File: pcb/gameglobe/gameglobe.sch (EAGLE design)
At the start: 12 parts

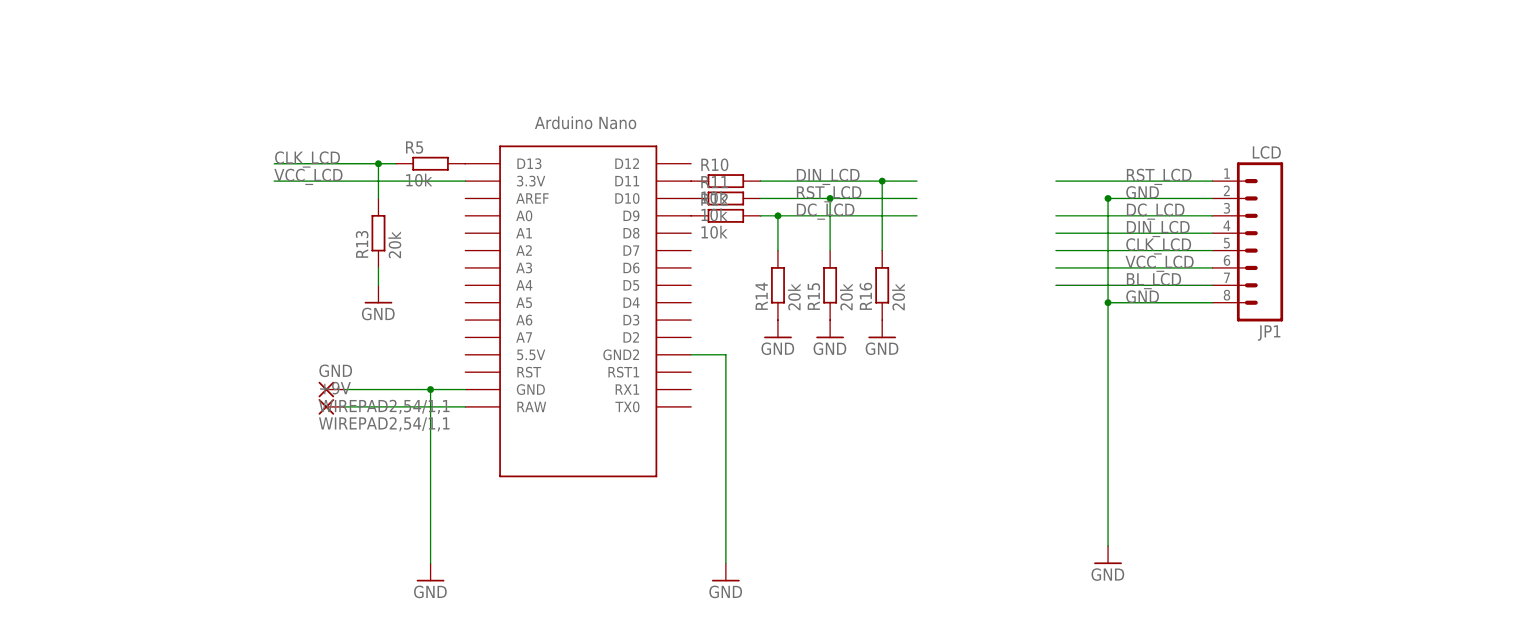
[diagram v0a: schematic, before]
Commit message: BOM is sortof complete, and PCB is more complete-ish now
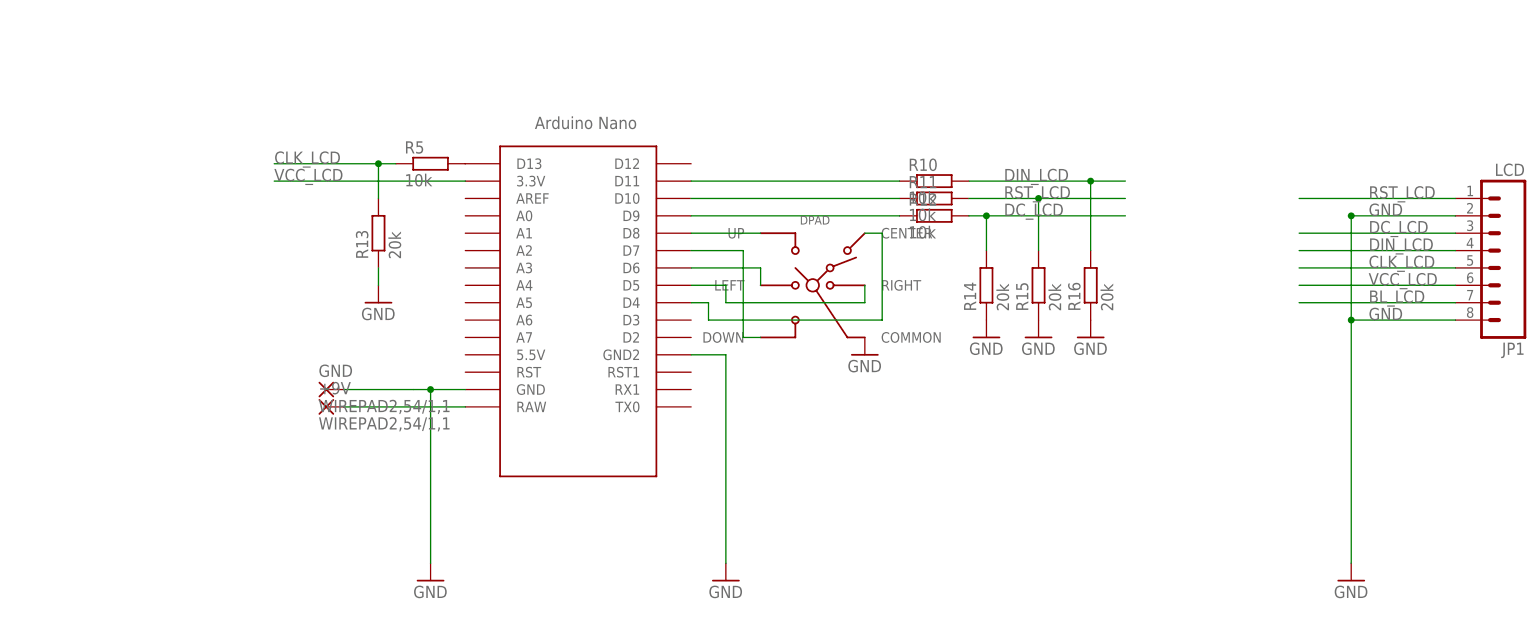
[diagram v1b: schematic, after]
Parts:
- added DPAD: SKQUCAA010, gamaral:SKQUCAA010
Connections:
- new net N$10: DPAD.CENTER, U$1.D4
- new net N$5: DPAD.UP, U$1.D8
- new net N$6: DPAD.DOWN, U$1.D7
- new net N$8: DPAD.LEFT, U$1.D6
- new net N$9: DPAD.RIGHT, U$1.D5
- net GND: now also DPAD.COMMON
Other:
- moved on the sheet: JP1, R10, R11, R12, R14, R15, R16

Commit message: Add backlight wire and resistor
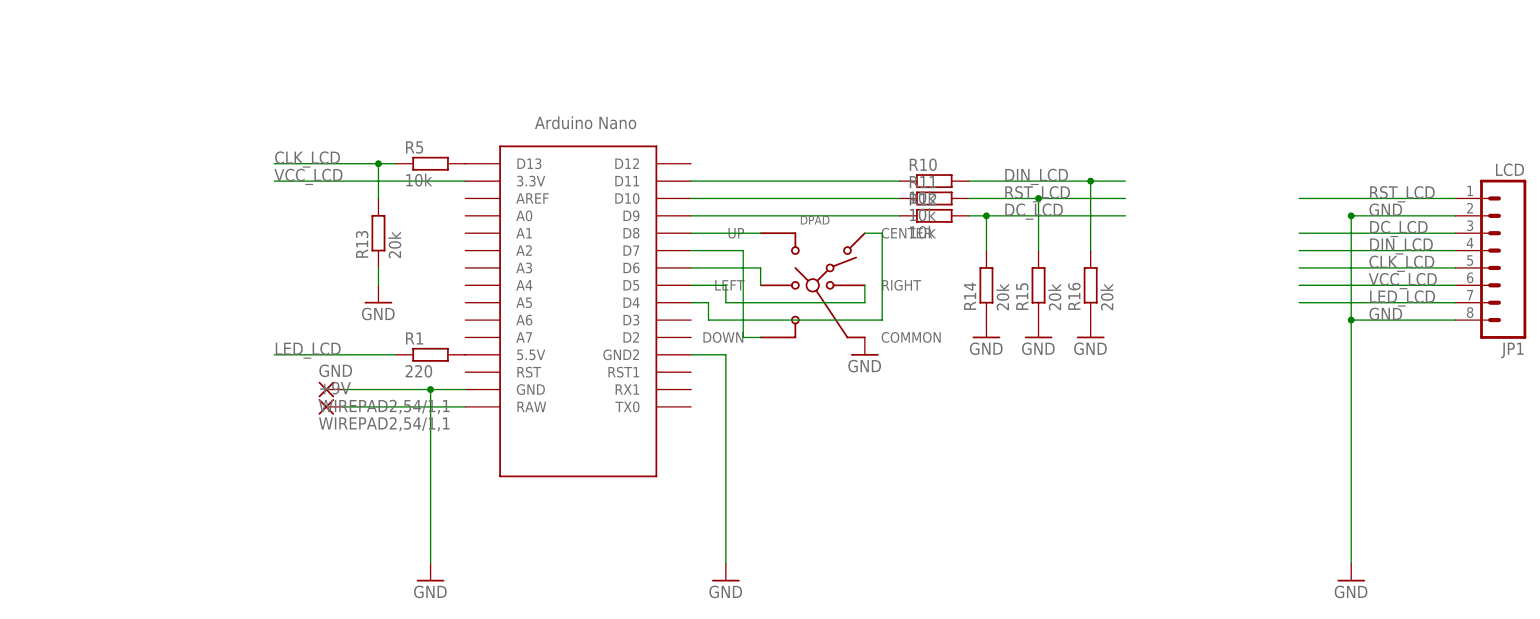
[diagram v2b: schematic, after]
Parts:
- added R1: 220, resistor:R-EU_0207/10
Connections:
- removed net BL_LCD: JP1.7
- new net LED_LCD: JP1.7, R1.1
- new net N$11: R1.2, U$1.5.5V
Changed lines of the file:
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@@
 <part name="DPAD" library="gamaral" deviceset="SKQU" device="CAA010"/>
 <part name="GND8" library="supply1" deviceset="GND" device=""/>
+<part name="R1" library="resistor" deviceset="R-EU_" device="0207/10" value="220"/>
 </parts>
 <sheets>
@@
 <instance part="DPAD" gate="Q$1" x="88.9" y="50.8"/>
 <instance part="GND8" gate="1" x="96.52" y="40.64"/>
+<instance part="R1" gate="G$1" x="33.02" y="40.64"/>
 </instances>
 <busses>
@@
 </segment>
 </net>
-<net name="BL_LCD" class="0">
+<net name="LED_LCD" class="0">
 <segment>
 <pinref part="JP1" gate="G$1" pin="7"/>
 <wire x1="182.88" y1="48.26" x2="160.02" y2="48.26" width="0.1524" layer="91"/>
 <label x="170.18" y="48.26" size="1.778" layer="95"/>
+</segment>
+<segment>
+<pinref part="R1" gate="G$1" pin="1"/>
+<wire x1="27.94" y1="40.64" x2="10.16" y2="40.64" width="0.1524" layer="91"/>
+<label x="10.16" y="40.64" size="1.778" layer="95"/>
 </segment>
 </net>
@@
 </segment>
 </net>
+<net name="N$11" class="0">
+<segment>
+<pinref part="U$1" gate="G$1" pin="5.5V"/>
+<pinref part="R1" gate="G$1" pin="2"/>
+</segment>
+</net>

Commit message: Improve net names and board layout
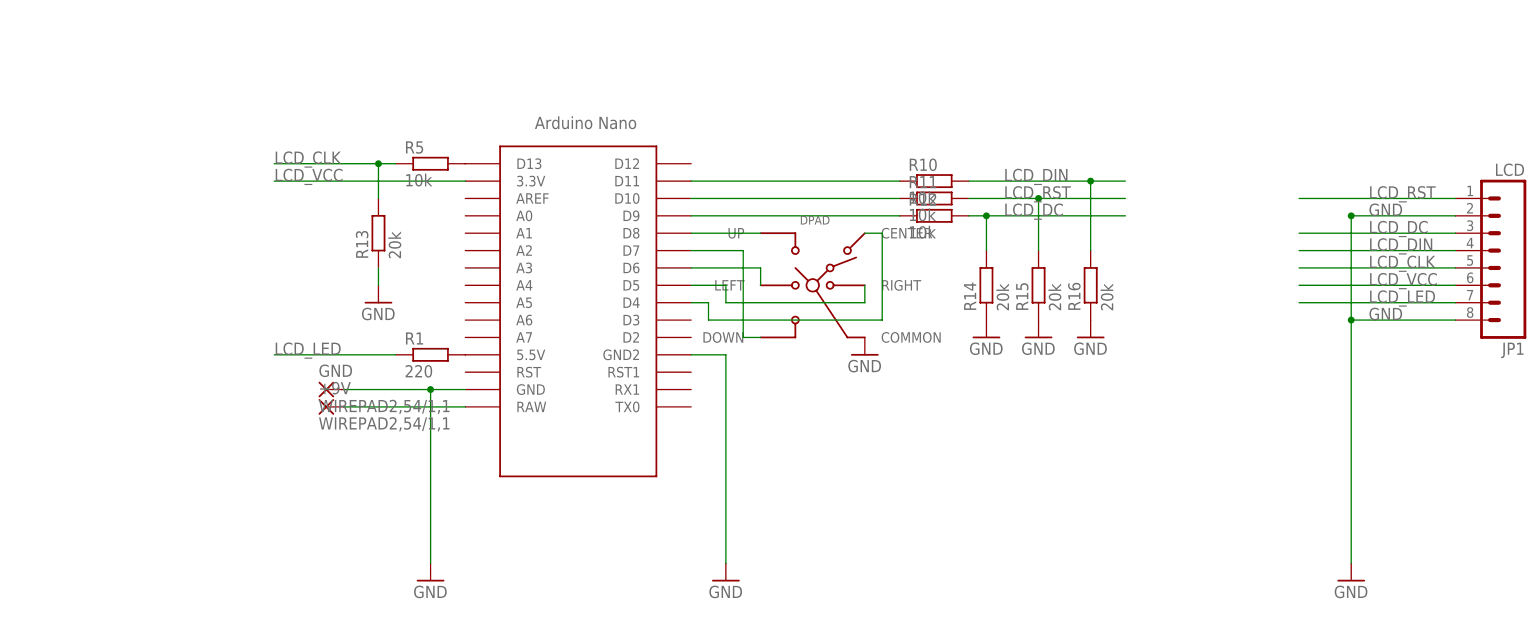
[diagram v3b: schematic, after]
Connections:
- net CLK_LCD renamed LCD_CLK
- net DC_LCD renamed LCD_DC
- net DIN_LCD renamed LCD_DIN
- net LED_LCD renamed LCD_LED
- net N$10 renamed DPAD_CENTER
- net N$5 renamed DPAD_UP
- net N$6 renamed DPAD_DOWN
- net N$8 renamed DPAD_LEFT
- net N$9 renamed DPAD_RIGHT
- net RST_LCD renamed LCD_RST
- net VCC_LCD renamed LCD_VCC
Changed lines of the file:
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@@
 </segment>
 </net>
-<net name="RST_LCD" class="0">
+<net name="LCD_RST" class="0">
 <segment>
 <pinref part="JP1" gate="G$1" pin="1"/>
@@
 </segment>
 </net>
-<net name="DC_LCD" class="0">
+<net name="LCD_DC" class="0">
 <segment>
 <pinref part="JP1" gate="G$1" pin="3"/>
@@
 </segment>
 </net>
-<net name="DIN_LCD" class="0">
+<net name="LCD_DIN" class="0">
 <segment>
 <pinref part="JP1" gate="G$1" pin="4"/>
@@
 </segment>
 </net>
-<net name="CLK_LCD" class="0">
+<net name="LCD_CLK" class="0">
 <segment>
 <pinref part="JP1" gate="G$1" pin="5"/>
@@
 </segment>
 </net>
-<net name="VCC_LCD" class="0">
+<net name="LCD_VCC" class="0">
 <segment>
 <pinref part="JP1" gate="G$1" pin="6"/>
@@
 </segment>
 </net>
-<net name="LED_LCD" class="0">
+<net name="LCD_LED" class="0">
 <segment>
 <pinref part="JP1" gate="G$1" pin="7"/>
@@
 </segment>
 </net>
-<net name="N$5" class="0">
+<net name="DPAD_UP" class="0">
 <segment>
 <pinref part="U$1" gate="G$1" pin="D8"/>
@@
 </segment>
 </net>
-<net name="N$6" class="0">
+<net name="DPAD_DOWN" class="0">
 <segment>
 <pinref part="DPAD" gate="Q$1" pin="DOWN"/>
@@
 </segment>
 </net>
-<net name="N$8" class="0">
+<net name="DPAD_LEFT" class="0">
 <segment>
 <pinref part="DPAD" gate="Q$1" pin="LEFT"/>
@@
 </segment>
 </net>
-<net name="N$9" class="0">
+<net name="DPAD_RIGHT" class="0">
 <segment>
 <pinref part="DPAD" gate="Q$1" pin="RIGHT"/>
@@
 </segment>
 </net>
-<net name="N$10" class="0">
+<net name="DPAD_CENTER" class="0">
 <segment>
 <pinref part="DPAD" gate="Q$1" pin="CENTER"/>

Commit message: Updated DRU file; Improved PCB layout; Added rounded edges and mount holes
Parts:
- renumbered U$1 to ARDUINO_NANO
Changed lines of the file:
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@@
 </classes>
 <parts>
-<part name="U$1" library="Arduino-clone" deviceset="NANO" device=""/>
+<part name="ARDUINO_NANO" library="Arduino-clone" deviceset="NANO" device=""/>
 <part name="+9V" library="wirepad" deviceset="WIREPAD" device="2,54/1,1"/>
 <part name="GND" library="wirepad" deviceset="WIREPAD" device="2,54/1,1"/>
@@
 </plain>
 <instances>
-<instance part="U$1" gate="G$1" x="60.96" y="53.34"/>
+<instance part="ARDUINO_NANO" gate="G$1" x="60.96" y="53.34"/>
 <instance part="+9V" gate="G$1" x="17.78" y="33.02"/>
 <instance part="GND" gate="G$1" x="17.78" y="35.56"/>
@@
 <net name="N$7" class="0">
 <segment>
-<pinref part="U$1" gate="G$1" pin="RAW"/>
+<pinref part="ARDUINO_NANO" gate="G$1" pin="RAW"/>
 <wire x1="38.1" y1="33.02" x2="20.32" y2="33.02" width="0.1524" layer="91"/>
 <pinref part="+9V" gate="G$1" pin="P"/>
@@
 <segment>
 <pinref part="GND1" gate="1" pin="GND"/>
-<pinref part="U$1" gate="G$1" pin="GND2"/>
+<pinref part="ARDUINO_NANO" gate="G$1" pin="GND2"/>
 <wire x1="71.12" y1="40.64" x2="76.2" y2="40.64" width="0.1524" layer="91"/>
 <wire x1="76.2" y1="40.64" x2="76.2" y2="10.16" width="0.1524" layer="91"/>
 </segment>
 <segment>
-<pinref part="U$1" gate="G$1" pin="GND"/>
+<pinref part="ARDUINO_NANO" gate="G$1" pin="GND"/>
 <wire x1="20.32" y1="35.56" x2="30.48" y2="35.56" width="0.1524" layer="91"/>
 <pinref part="GND2" gate="1" pin="GND"/>
@@
 </segment>
 <segment>
-<pinref part="U$1" gate="G$1" pin="3.3V"/>
+<pinref part="ARDUINO_NANO" gate="G$1" pin="3.3V"/>
 <label x="10.16" y="66.04" size="1.778" layer="95"/>
 <wire x1="38.1" y1="66.04" x2="10.16" y2="66.04" width="0.1524" layer="91"/>
@@
 <net name="N$1" class="0">
 <segment>
-<pinref part="U$1" gate="G$1" pin="D13"/>
+<pinref part="ARDUINO_NANO" gate="G$1" pin="D13"/>
 <pinref part="R5" gate="G$1" pin="2"/>
 </segment>
@@
 <net name="N$2" class="0">
 <segment>
-<pinref part="U$1" gate="G$1" pin="D11"/>
+<pinref part="ARDUINO_NANO" gate="G$1" pin="D11"/>
 <pinref part="R10" gate="G$1" pin="1"/>
 <wire x1="101.6" y1="66.04" x2="71.12" y2="66.04" width="0.1524" layer="91"/>
@@
 <net name="N$3" class="0">
 <segment>
-<pinref part="U$1" gate="G$1" pin="D10"/>
+<pinref part="ARDUINO_NANO" gate="G$1" pin="D10"/>
 <pinref part="R11" gate="G$1" pin="1"/>
 <wire x1="101.6" y1="63.5" x2="71.12" y2="63.5" width="0.1524" layer="91"/>
@@
 <net name="N$4" class="0">
 <segment>
-<pinref part="U$1" gate="G$1" pin="D9"/>
+<pinref part="ARDUINO_NANO" gate="G$1" pin="D9"/>
 <pinref part="R12" gate="G$1" pin="1"/>
 <wire x1="101.6" y1="60.96" x2="71.12" y2="60.96" width="0.1524" layer="91"/>
@@
 <net name="DPAD_UP" class="0">
 <segment>
-<pinref part="U$1" gate="G$1" pin="D8"/>
+<pinref part="ARDUINO_NANO" gate="G$1" pin="D8"/>
 <pinref part="DPAD" gate="Q$1" pin="UP"/>
 <wire x1="71.12" y1="58.42" x2="81.28" y2="58.42" width="0.1524" layer="91"/>
@@
 <wire x1="81.28" y1="43.18" x2="78.74" y2="43.18" width="0.1524" layer="91"/>
 <wire x1="78.74" y1="43.18" x2="78.74" y2="55.88" width="0.1524" layer="91"/>
-<pinref part="U$1" gate="G$1" pin="D7"/>
+<pinref part="ARDUINO_NANO" gate="G$1" pin="D7"/>
 <wire x1="78.74" y1="55.88" x2="71.12" y2="55.88" width="0.1524" layer="91"/>
 </segment>
@@
 <pinref part="DPAD" gate="Q$1" pin="LEFT"/>
 <wire x1="81.28" y1="50.8" x2="81.28" y2="53.34" width="0.1524" layer="91"/>
-<pinref part="U$1" gate="G$1" pin="D6"/>
+<pinref part="ARDUINO_NANO" gate="G$1" pin="D6"/>
 <wire x1="81.28" y1="53.34" x2="71.12" y2="53.34" width="0.1524" layer="91"/>
 </segment>
@@
 <wire x1="96.52" y1="48.26" x2="76.2" y2="48.26" width="0.1524" layer="91"/>
 <wire x1="76.2" y1="48.26" x2="76.2" y2="50.8" width="0.1524" layer="91"/>
-<pinref part="U$1" gate="G$1" pin="D5"/>
+<pinref part="ARDUINO_NANO" gate="G$1" pin="D5"/>
 <wire x1="76.2" y1="50.8" x2="71.12" y2="50.8" width="0.1524" layer="91"/>
 </segment>
@@
 <wire x1="99.06" y1="45.72" x2="73.66" y2="45.72" width="0.1524" layer="91"/>
 <wire x1="73.66" y1="45.72" x2="73.66" y2="48.26" width="0.1524" layer="91"/>
-<pinref part="U$1" gate="G$1" pin="D4"/>
+<pinref part="ARDUINO_NANO" gate="G$1" pin="D4"/>
 <wire x1="73.66" y1="48.26" x2="71.12" y2="48.26" width="0.1524" layer="91"/>
 </segment>
@@
 <net name="N$11" class="0">
 <segment>
-<pinref part="U$1" gate="G$1" pin="5.5V"/>
+<pinref part="ARDUINO_NANO" gate="G$1" pin="5.5V"/>
 <pinref part="R1" gate="G$1" pin="2"/>
 </segment>

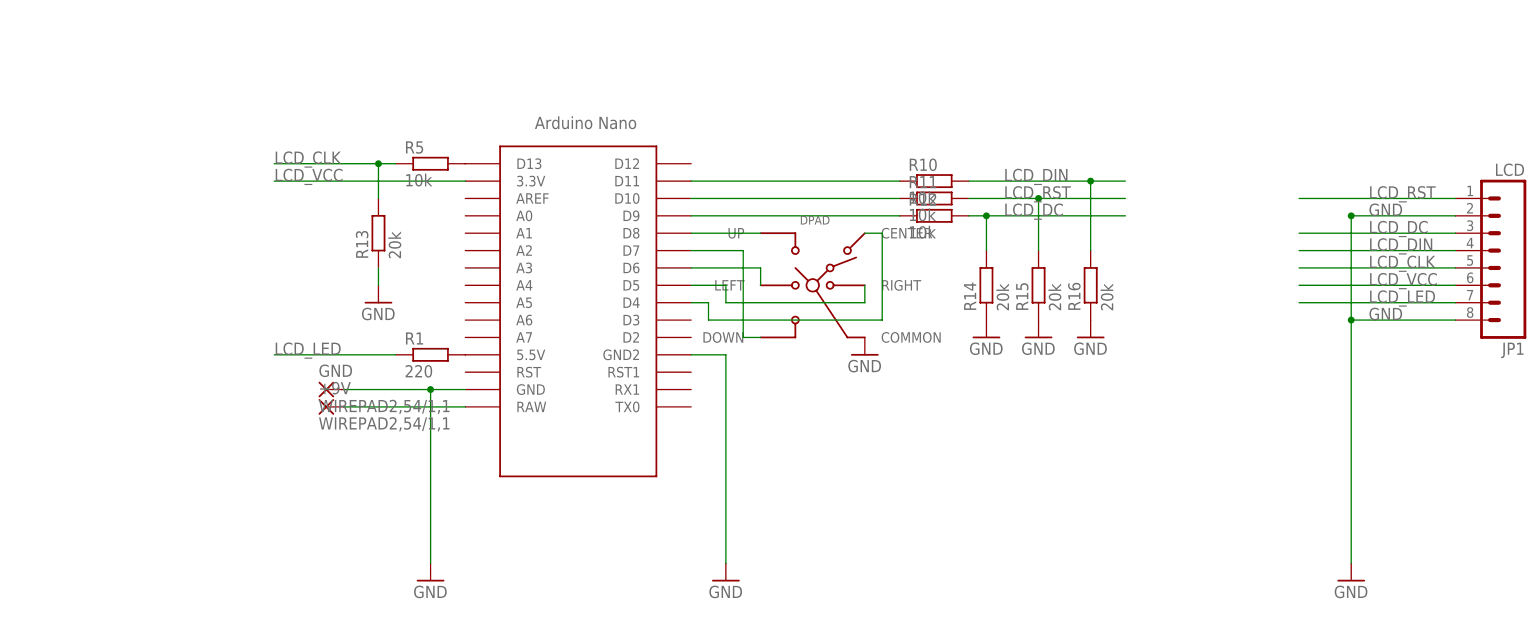
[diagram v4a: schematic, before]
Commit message: Many PCB improvements. Actually the first version where everything (joystick, lcd, nano) is centered on the board
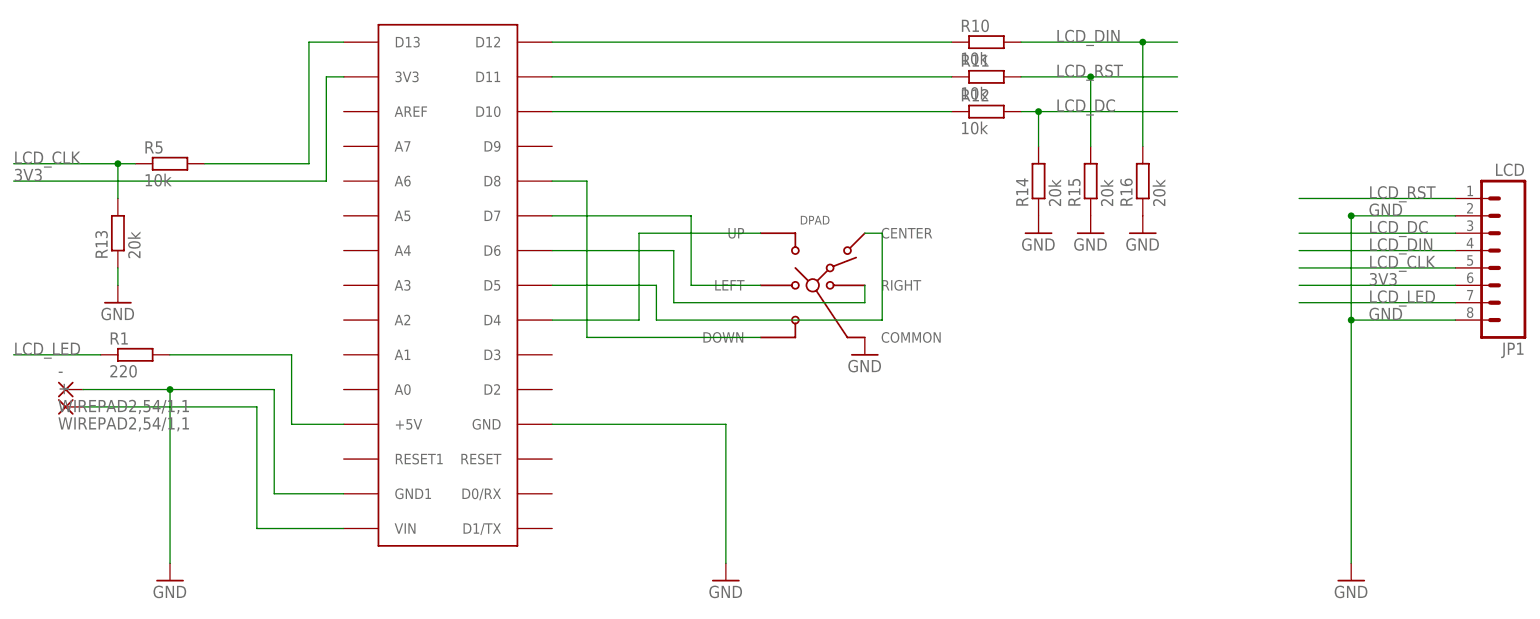
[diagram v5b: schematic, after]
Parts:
- removed +9V, GND: WIREPAD2,54/1,1, wirepad:WIREPAD2,54/1,1
- removed ARDUINO_NANO: NANO, Arduino-clone:NANO
- added +, -: WIREPAD2,54/1,1, wirepad:WIREPAD2,54/1,1
- added U$5: ARDUINONANO, jet-lib:ARDUINONANO
- R1, R10, R11, R12, R13, R14, R15, R16, R5: device resistor:R-EU_0207/10 -> resistor:R-EU_0411/15
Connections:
- removed net DPAD_DOWN: ARDUINO_NANO.D7, DPAD.DOWN
- removed net DPAD_UP: ARDUINO_NANO.D8, DPAD.UP
- removed net LCD_VCC: ARDUINO_NANO.3.3V, JP1.6
- removed net N$11: ARDUINO_NANO.5.5V, R1.2
- new net 3V3: JP1.6, U$5.3V3
- new net 5V: R1.2, U$5.+5V
- new net N$5: DPAD.DOWN, U$5.D8
- new net N$6: DPAD.UP, U$5.D4
- net DPAD_CENTER: now also U$5.D5; no longer ARDUINO_NANO.D4
- net DPAD_LEFT: now also U$5.D7; no longer ARDUINO_NANO.D6
- net DPAD_RIGHT: now also U$5.D6; no longer ARDUINO_NANO.D5
- net GND: now also -.P, U$5.GND, U$5.GND1; no longer ARDUINO_NANO.GND, ARDUINO_NANO.GND2, GND.P
- net N$1: now also U$5.D13; no longer ARDUINO_NANO.D13
- net N$2: now also U$5.D12; no longer ARDUINO_NANO.D11
- net N$3: now also U$5.D11; no longer ARDUINO_NANO.D10
- net N$4: now also U$5.D10; no longer ARDUINO_NANO.D9
- net N$7: now also +.P, U$5.VIN; no longer +9V.P, ARDUINO_NANO.RAW
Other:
- moved on the sheet: R1, R10, R11, R12, R13, R14, R15, R16, R5
